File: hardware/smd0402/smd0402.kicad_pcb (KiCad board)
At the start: 2 copper layers, 150 x 146.5 mm, 140 parts, among them J1 Conn_01x03, J2 SAO v1.69bis addon, J3 SAO v1.69bis badge, P1 Conn_01x02, P2 Conn_01x02, P3 Conn_01x02, P4 Conn_01x02, P5 Conn_01x02, P6 Conn_01x02, U1 WCH CH32V003F4U6

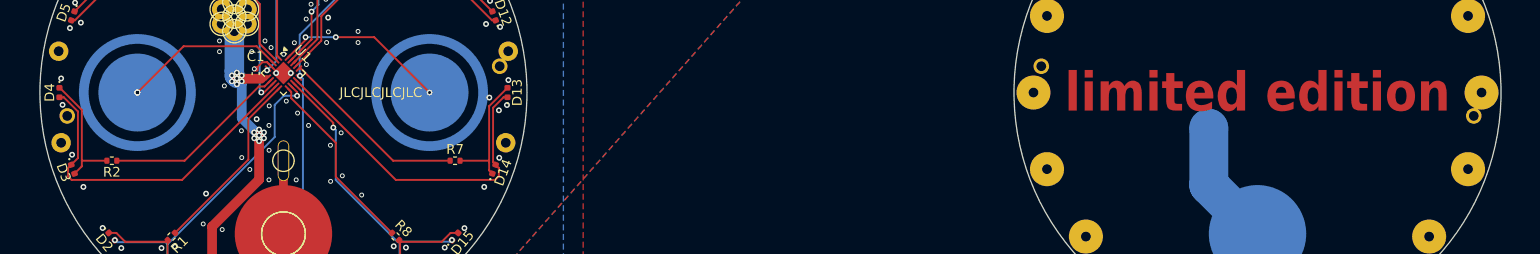
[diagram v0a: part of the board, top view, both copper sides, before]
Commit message: add 2 alignment holes to each outer layer
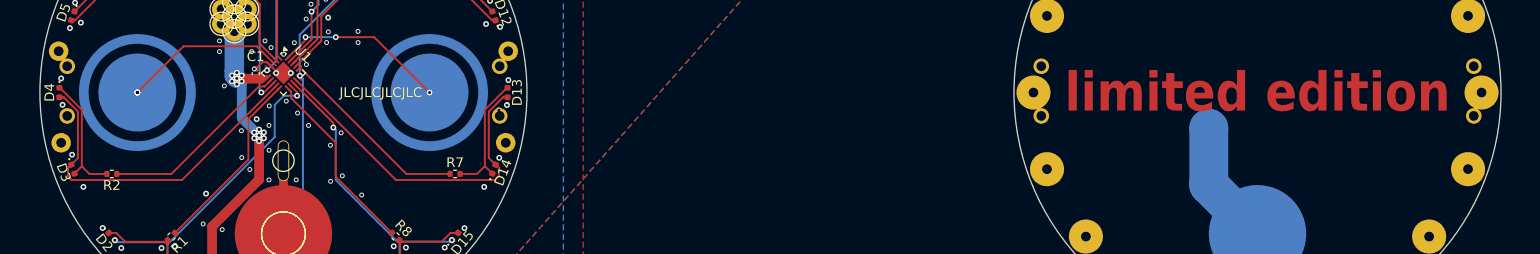
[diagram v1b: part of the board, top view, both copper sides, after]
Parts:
- added align-o2: , , F.Cu at (172.2, 47.3)
- added align-o3: , , F.Cu at (127.8, 52.4)
- added align-r1: , , F.Cu at (27.8, 47.3)
- added align-r4: , , F.Cu at (72.2, 52.4)
- moved R2 1.36 mm to (32.4, 58.4)
- moved R7 1.36 mm to (67.6, 58.4)
- renumbered align-io1 to align-i1, align-ir2 to align-i2, align-ir1 to align-i3, align-io2 to align-i4, align-o2 to align-o4, align-r1 to align-r3
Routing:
- net PWM7: track 19.4 -> 20.0 mm
- net PWM2: track 19.2 -> 19.8 mm
- net GND: vias 118 -> 117

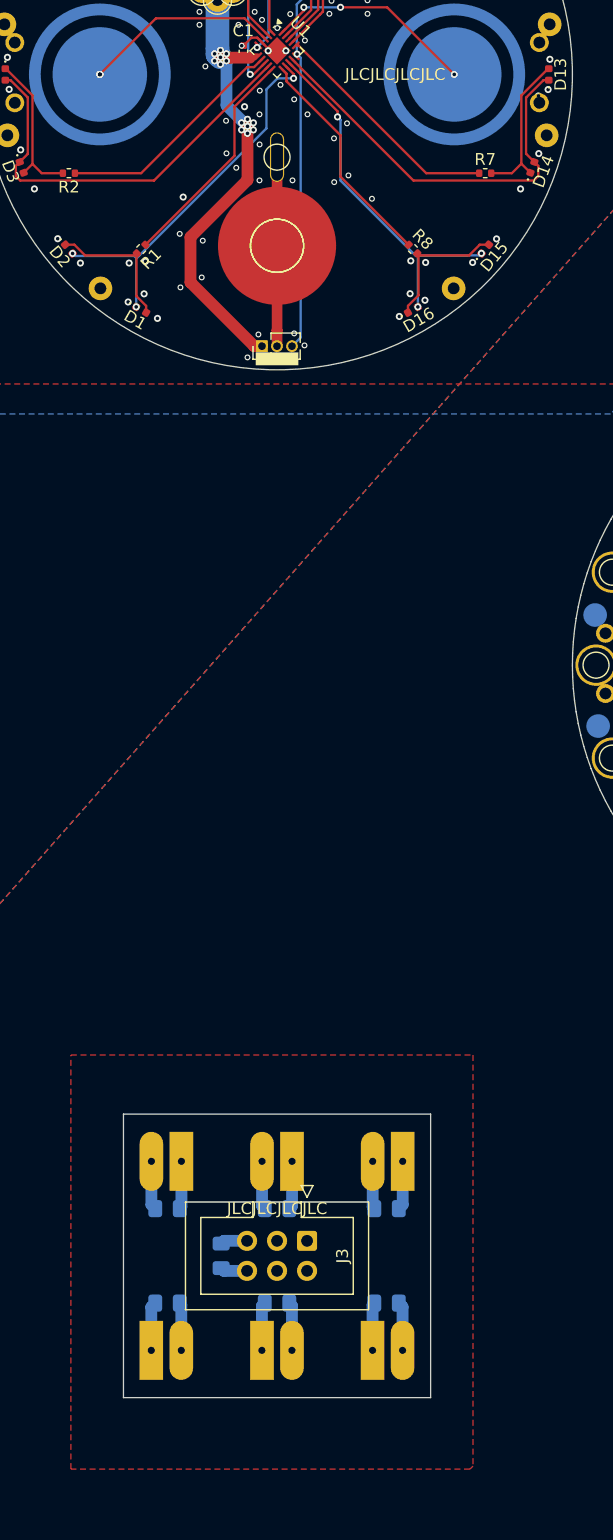
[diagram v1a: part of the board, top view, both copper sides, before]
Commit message: remove SAO display
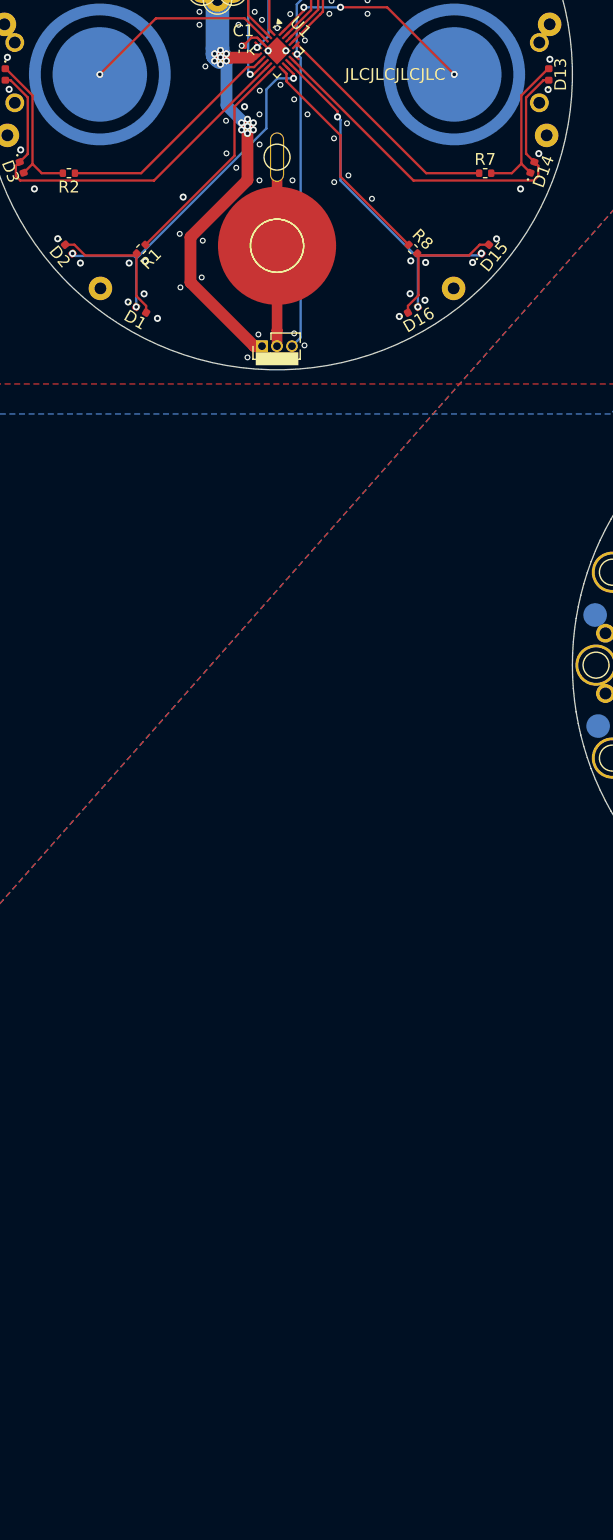
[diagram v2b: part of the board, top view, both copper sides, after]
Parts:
- removed BC1, BC2, BC3, BC4, BC5, BC6, BC7: 1u, Capacitor_SMD:C_0805_2012Metric_Pad1.18x1.45mm_HandSolder
- removed J3: SAO v1.69bis badge, Connector_IDC:IDC-Header_2x03_P2.54mm_Vertical
- removed P1, P2, P3, P4, P5, P6: Conn_01x02, Connector_PinHeader_2.54mm:PinHeader_1x02_P2.54mm_Vertical
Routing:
- net +3V0: track 112.0 -> 85.1 mm
- net GND: track 68.3 -> 41.4 mm, vias 117 -> 116
- net /touch2: vias 3 -> 1
- removed copper zone on F.Cu, net +3V0
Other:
- outline, holes or cut-outs redrawn

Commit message: change text
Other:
- board text added: "E PLVRIBVS VNVM"
- board text removed: "limited edition"
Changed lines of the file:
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@@
 	)
 	(footprint "TestPoint:TestPoint_THTPad_D1.0mm_Drill0.5mm"
-		(locked yes)
 		(layer "F.Cu")
 		(at 127 50)
@@
 			)
 		)
-		(attr board_only exclude_from_pos_files exclude_from_bom)
+		(attr board_only exclude_from_pos_files exclude_from_bom dnp)
 		(fp_circle
 			(center 0 0)
@@
 	)
 	(footprint "TestPoint:TestPoint_THTPad_D1.0mm_Drill0.5mm"
-		(locked yes)
 		(layer "F.Cu")
 		(at 128.387 57.866)
@@
 			)
 		)
-		(attr board_only exclude_from_pos_files exclude_from_bom)
+		(attr board_only exclude_from_pos_files exclude_from_bom dnp)
 		(fp_circle
 			(center 0 0)
@@
 	)
 	(footprint "TestPoint:TestPoint_THTPad_D1.0mm_Drill0.5mm"
-		(locked yes)
 		(layer "F.Cu")
 		(at 167.619 64.784)
@@
 			)
 		)
-		(attr board_only exclude_from_pos_files exclude_from_bom)
+		(attr board_only exclude_from_pos_files exclude_from_bom dnp)
 		(fp_circle
 			(center 0 0)
@@
 	)
 	(footprint ""
-		(locked yes)
 		(layer "F.Cu")
 		(at 172.2 52.4)
@@
 	)
 	(footprint ""
-		(locked yes)
 		(layer "F.Cu")
 		(at 127.8 52.4)
@@
 	)
 	(footprint "TestPoint:TestPoint_THTPad_D1.0mm_Drill0.5mm"
-		(locked yes)
 		(layer "F.Cu")
 		(at 167.619 35.2159)
@@
 			)
 		)
-		(attr board_only exclude_from_pos_files exclude_from_bom)
+		(attr board_only exclude_from_pos_files exclude_from_bom dnp)
 		(fp_circle
 			(center 0 0)
@@
 	)
 	(footprint "TestPoint:TestPoint_THTPad_D1.0mm_Drill0.5mm"
-		(locked yes)
 		(layer "F.Cu")
 		(at 146.006 27.3494)
@@
 			)
 		)
-		(attr board_only exclude_from_pos_files exclude_from_bom)
+		(attr board_only exclude_from_pos_files exclude_from_bom dnp)
 		(fp_circle
 			(center 0 0)
@@
 	)
 	(footprint "TestPoint:TestPoint_THTPad_D1.0mm_Drill0.5mm"
-		(locked yes)
 		(layer "F.Cu")
 		(at 161.5 69.919)
@@
 			)
 		)
-		(attr board_only exclude_from_pos_files exclude_from_bom)
+		(attr board_only exclude_from_pos_files exclude_from_bom dnp)
 		(fp_circle
 			(center 0 0)
@@
 	)
 	(footprint "TestPoint:TestPoint_THTPad_D1.0mm_Drill0.5mm"
-		(locked yes)
 		(layer "F.Cu")
 		(at 128.387 42.1335)
@@
 			)
 		)
-		(attr board_only exclude_from_pos_files exclude_from_bom)
+		(attr board_only exclude_from_pos_files exclude_from_bom dnp)
 		(fp_circle
 			(center 0 0)
@@
 	)
 	(footprint "TestPoint:TestPoint_THTPad_D1.0mm_Drill0.5mm"
-		(locked yes)
 		(layer "F.Cu")
 		(at 138.5 30.0814)
@@
 			)
 		)
-		(attr board_only exclude_from_pos_files exclude_from_bom)
+		(attr board_only exclude_from_pos_files exclude_from_bom dnp)
 		(fp_circle
 			(center 0 0)
@@
 	)
 	(footprint "TestPoint:TestPoint_THTPad_D1.0mm_Drill0.5mm"
-		(locked yes)
 		(layer "F.Cu")
 		(at 173 50)
@@
 			)
 		)
-		(attr board_only exclude_from_pos_files exclude_from_bom)
+		(attr board_only exclude_from_pos_files exclude_from_bom dnp)
 		(fp_circle
 			(center 0 0)
@@
 	)
 	(footprint ""
-		(locked yes)
 		(layer "F.Cu")
 		(at 172.2 47.3)
@@
 	)
 	(footprint "TestPoint:TestPoint_THTPad_D1.0mm_Drill0.5mm"
-		(locked yes)
 		(layer "F.Cu")
 		(at 171.613 57.866)
@@
 			)
 		)
-		(attr board_only exclude_from_pos_files exclude_from_bom)
+		(attr board_only exclude_from_pos_files exclude_from_bom dnp)
 		(fp_circle
 			(center 0 0)
@@
 	)
 	(footprint "TestPoint:TestPoint_THTPad_D1.0mm_Drill0.5mm"
-		(locked yes)
 		(layer "F.Cu")
 		(at 171.613 42.1335)
@@
 			)
 		)
-		(attr board_only exclude_from_pos_files exclude_from_bom)
+		(attr board_only exclude_from_pos_files exclude_from_bom dnp)
 		(fp_circle
 			(center 0 0)
@@
 	)
 	(footprint "TestPoint:TestPoint_THTPad_D1.0mm_Drill0.5mm"
-		(locked yes)
 		(layer "F.Cu")
 		(at 132.381 35.2159)
@@
 			)
 		)
-		(attr board_only exclude_from_pos_files exclude_from_bom)
+		(attr board_only exclude_from_pos_files exclude_from_bom dnp)
 		(fp_circle
 			(center 0 0)
@@
 	)
 	(footprint "TestPoint:TestPoint_THTPad_D1.0mm_Drill0.5mm"
-		(locked yes)
 		(layer "F.Cu")
 		(at 132.381 64.784)
@@
 			)
 		)
-		(attr board_only exclude_from_pos_files exclude_from_bom)
+		(attr board_only exclude_from_pos_files exclude_from_bom dnp)
 		(fp_circle
 			(center 0 0)
@@
 	)
 	(footprint "TestPoint:TestPoint_THTPad_D1.0mm_Drill0.5mm"
-		(locked yes)
 		(layer "F.Cu")
 		(at 153.994 27.3494)
@@
 			)
 		)
-		(attr board_only exclude_from_pos_files exclude_from_bom)
+		(attr board_only exclude_from_pos_files exclude_from_bom dnp)
 		(fp_circle
 			(center 0 0)
@@
 			)
 		)
-		(attr board_only exclude_from_pos_files exclude_from_bom)
+		(attr board_only exclude_from_pos_files exclude_from_bom dnp)
 		(fp_circle
 			(center 0 0)
@@
 	)
 	(footprint ""
-		(locked yes)
 		(layer "F.Cu")
 		(at 127.8 47.3)
@@
 	)
 	(footprint "TestPoint:TestPoint_THTPad_D1.0mm_Drill0.5mm"
-		(locked yes)
 		(layer "F.Cu")
 		(at 138.5 69.919)
@@
 			)
 		)
-		(attr board_only exclude_from_pos_files exclude_from_bom)
+		(attr board_only exclude_from_pos_files exclude_from_bom dnp)
 		(fp_circle
 			(center 0 0)
@@
 	)
 	(footprint "TestPoint:TestPoint_Pad_D4.0mm"
-		(locked yes)
 		(layer "B.Cu")
 		(at 144.996 53.67 180)
@@
 	)
 	(footprint "TestPoint:TestPoint_Pad_D4.0mm"
-		(locked yes)
 		(layer "B.Cu")
 		(at 150 64.5 180)
@@
 		(embedded_fonts no)
 	)
-	(gr_rect
-		(start 129.8 47.3)
-		(end 170.2 52.4)
-		(stroke
-			(width 1)
-			(type solid)
-		)
-		(fill yes)
-		(locked yes)
-		(layer "F.Mask")
-	)
 	(gr_circle
 		(center 35 50)
@@
 		)
 		(fill yes)
-		(locked yes)
 		(layer "F.SilkS")
 	)
@@
 		(layer "User.4")
 	)
-	(gr_text "limited edition"
-		(locked yes)
+	(gr_text "E PLVRIBVS VNVM"
 		(at 150 50 0)
 		(layer "F.Cu")
 		(effects
 			(font
-				(size 4 3.5)
+				(size 4 3)
 				(thickness 0.5)
 				(bold yes)
@@
 		(end 150 64.5)
 		(width 4)
-		(locked yes)
 		(layer "B.Cu")
 		(net 3)
@@
 		(end 144.996 59.496)
 		(width 4)
-		(locked yes)
 		(layer "B.Cu")
 		(net 3)

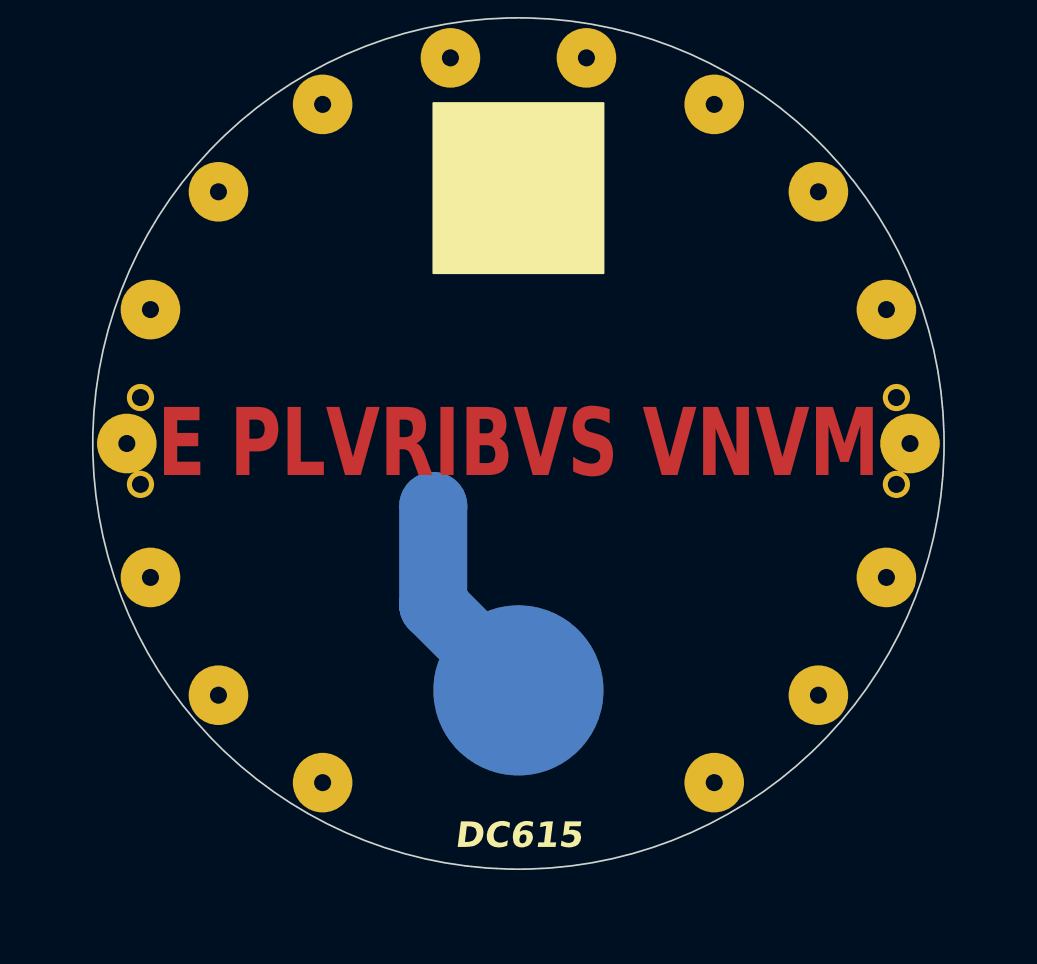
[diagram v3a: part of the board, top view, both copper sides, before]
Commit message: reduce maskless copper; tweak font
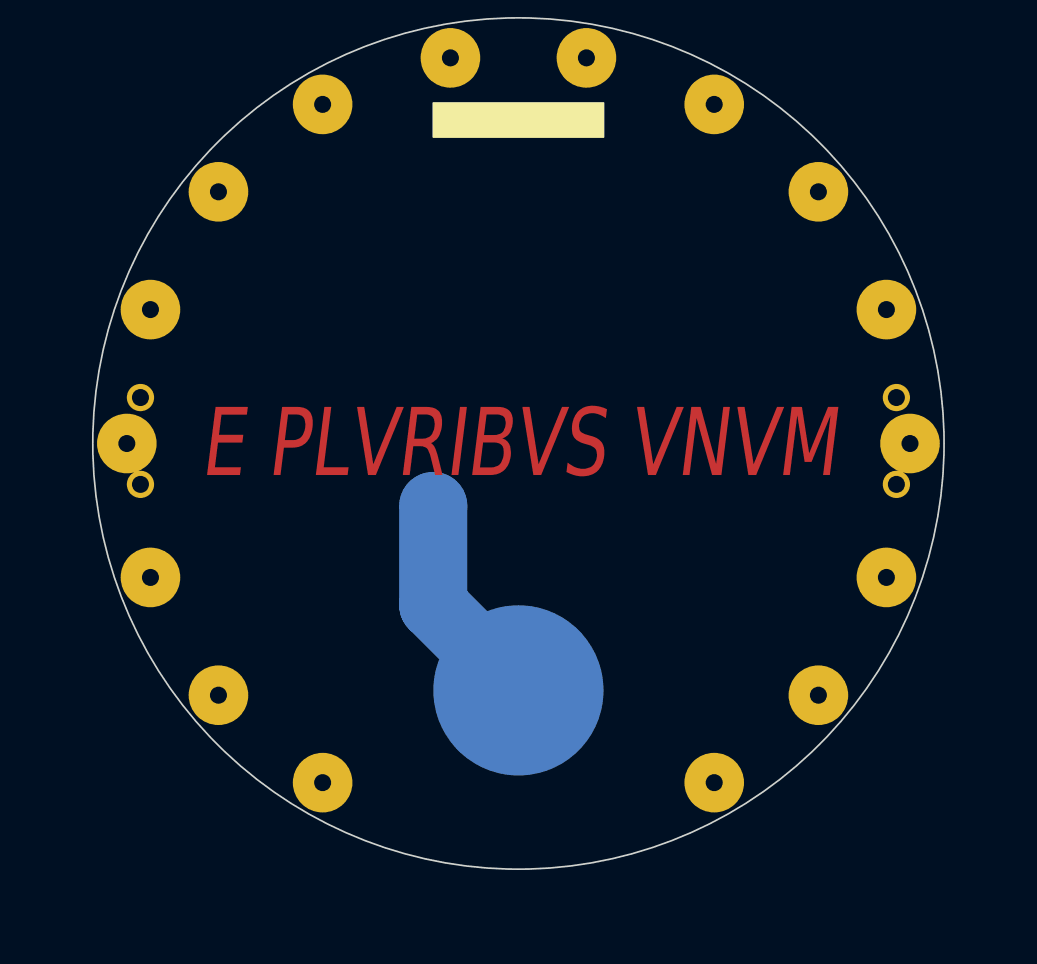
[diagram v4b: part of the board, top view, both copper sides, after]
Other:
- board text removed: "DC615"

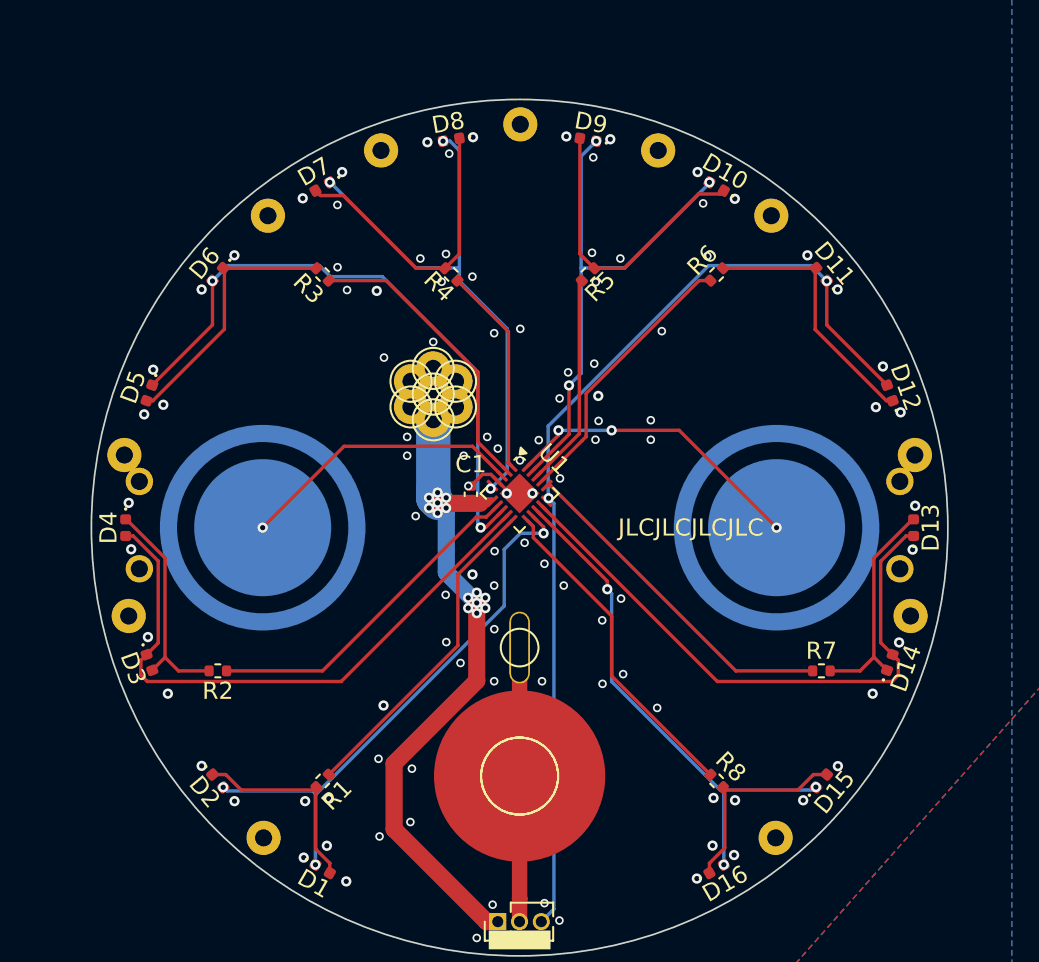
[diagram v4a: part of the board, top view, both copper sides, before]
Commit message: cleaned up pads; relocated repo QR
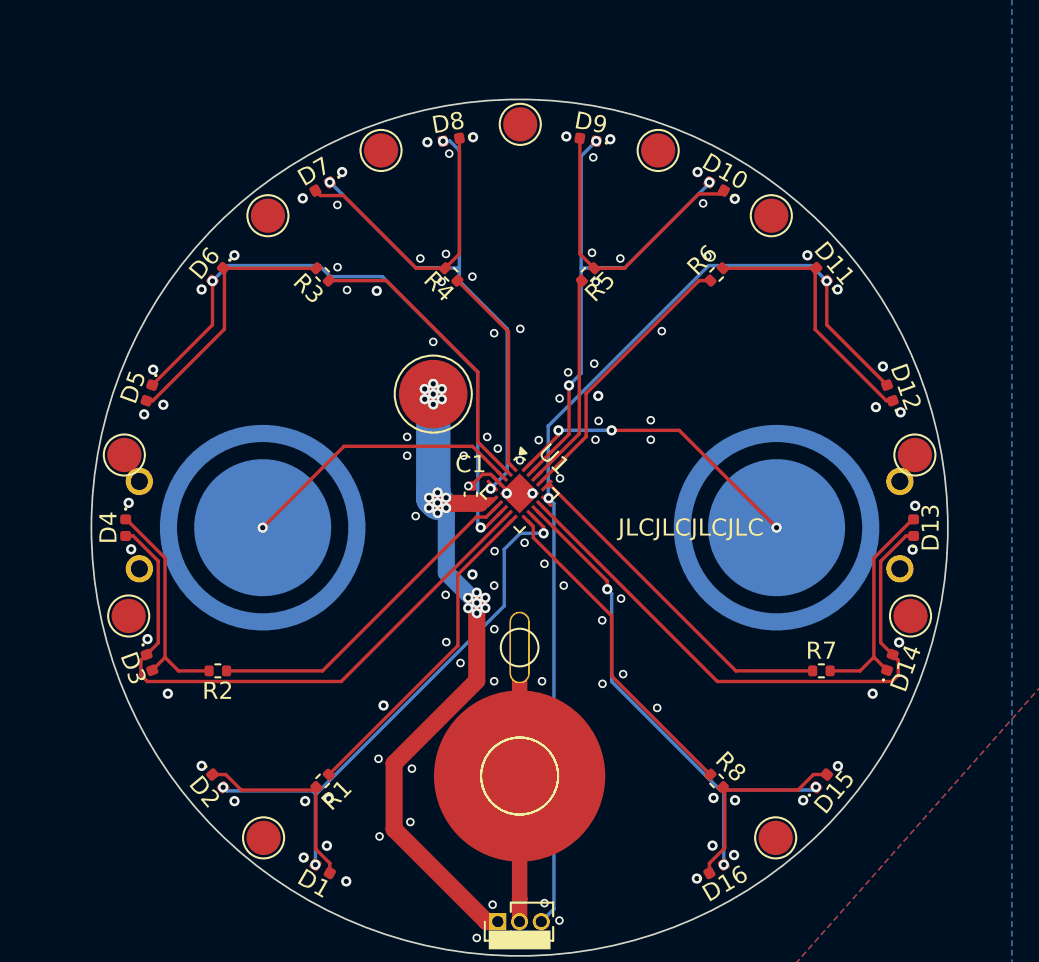
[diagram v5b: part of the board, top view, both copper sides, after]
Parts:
- removed through-r1, through-r2, through-r3, through-r4, through-r5, through-r6, through-r7: TestPoint_THTPad_D2.0mm_Drill1.0mm, TestPoint:TestPoint_THTPad_D2.0mm_Drill1.0mm
- added contact-r1: TestPoint_Pad_D4.0mm, TestPoint:TestPoint_Pad_D4.0mm, F.Cu at (45.0, 42.2)
- stitch1 (x11): value (none) -> TestPoint_Pad_D2.0mm; footprint (none) -> TestPoint:TestPoint_Pad_D2.0mm
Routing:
- net GND: vias 116 -> 115
- net +3V0: vias 14 -> 21

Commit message: integrated final assembly instructions
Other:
- board text added: "1. apply solder paste, stack internal board, reflow"
- board text added: "2. apply solder paste, reflow to thicken pad"
- board text added: "3. apply solder paste, reflow to thicken pad"
- board text added: "4. apply solder paste, stack upper sandwich, reflow"
